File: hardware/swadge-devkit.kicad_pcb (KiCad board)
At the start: 2 copper layers, 63.7 x 100 mm, 60 parts, among them J1 USB_B_Micro, SW1 SW_SPDT, SW2 4-1437565-2, SW3 4-1437565-2, SW4 4-1437565-2, SW5 4-1437565-2, U1 ESP-12F, U2 MCP6001-OT, U3 MSA300, U4 AP1117-33, U5 BUS_PCIexpress, U6 DISP_OLED_UG-2864HSWEG01, U9 MMA8452Q

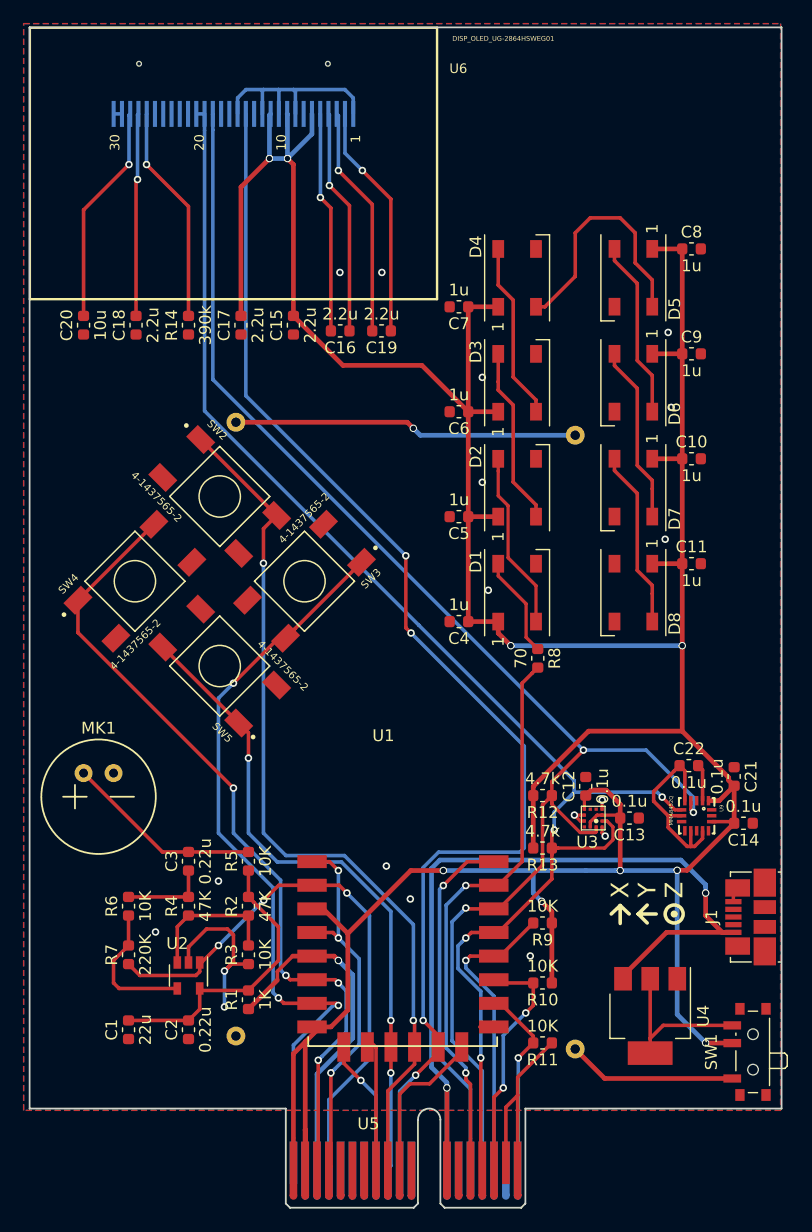
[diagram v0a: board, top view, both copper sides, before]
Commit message: Added SAO Moved mic out of the way of buttons Swapped 1.3" display for 0.96" display Linked vishay display instead of adafruit one
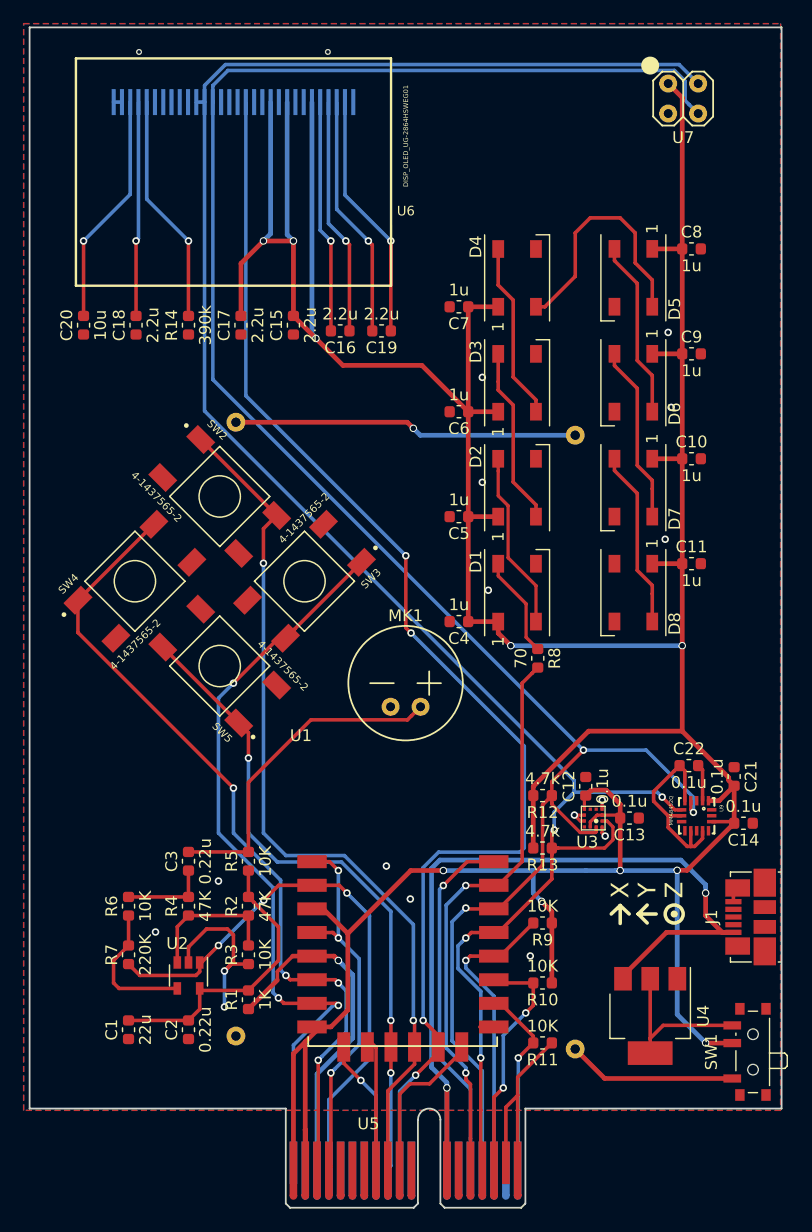
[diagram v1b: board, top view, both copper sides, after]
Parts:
- added U7: SAO, Swadge_Parts:SAO, F.Cu at (167.6, 52.1)
- U6: footprint Swadge_Parts:microbuilder-UG-2864HSWEG01_1.3_WRAPAROUND -> Swadge_Parts:microbuilder-UG-2864HSWEG01_0.96IN_WRAPAROUND
- moved MK1 27.7 mm to (145.4, 102.9), turned to 0 degrees
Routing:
- net SCL: track 129.1 -> 175.6 mm
- net SDA: track 126.9 -> 172.5 mm
- net +3V3: track 316.8 -> 349.8 mm, vias 9 -> 10
- net GND: track 74.9 -> 56.0 mm
- net Net-(C3-Pad2): track 16.7 -> 28.2 mm
- net Net-(C16-Pad1): track 19.1 -> 20.1 mm
- net Net-(C20-Pad2): track 18.8 -> 19.8 mm
- net Net-(C18-Pad2): track 17.2 -> 18.2 mm
- net MOSI: track 107.4 -> 108.4 mm
- net Net-(C19-Pad2): track 19.6 -> 20.6 mm
- net Net-(C19-Pad1): track 20.0 -> 21.0 mm
- net Net-(C16-Pad2): track 18.8 -> 19.8 mm
- net Net-(R14-Pad2): track 18.6 -> 19.6 mm
- net (no net): vias 2 -> 0

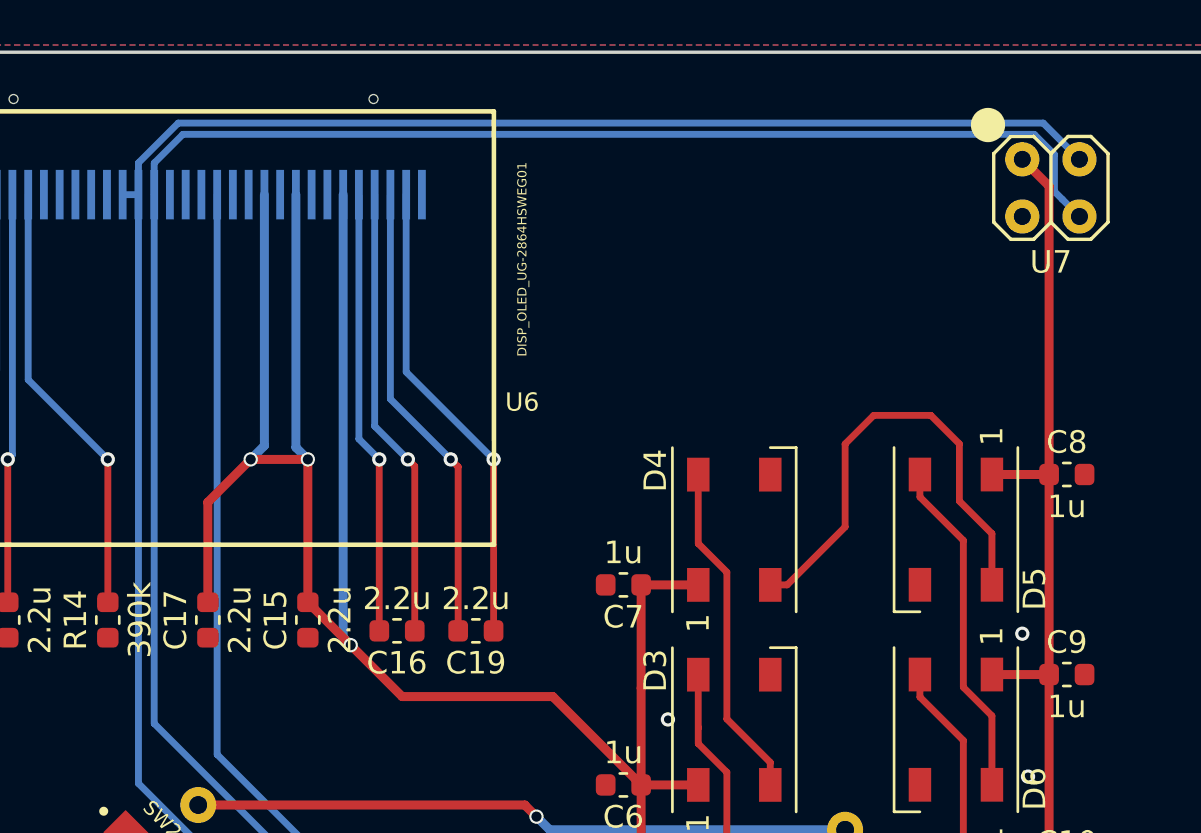
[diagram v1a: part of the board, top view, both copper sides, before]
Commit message: Added magfest logo & PCB color swatches
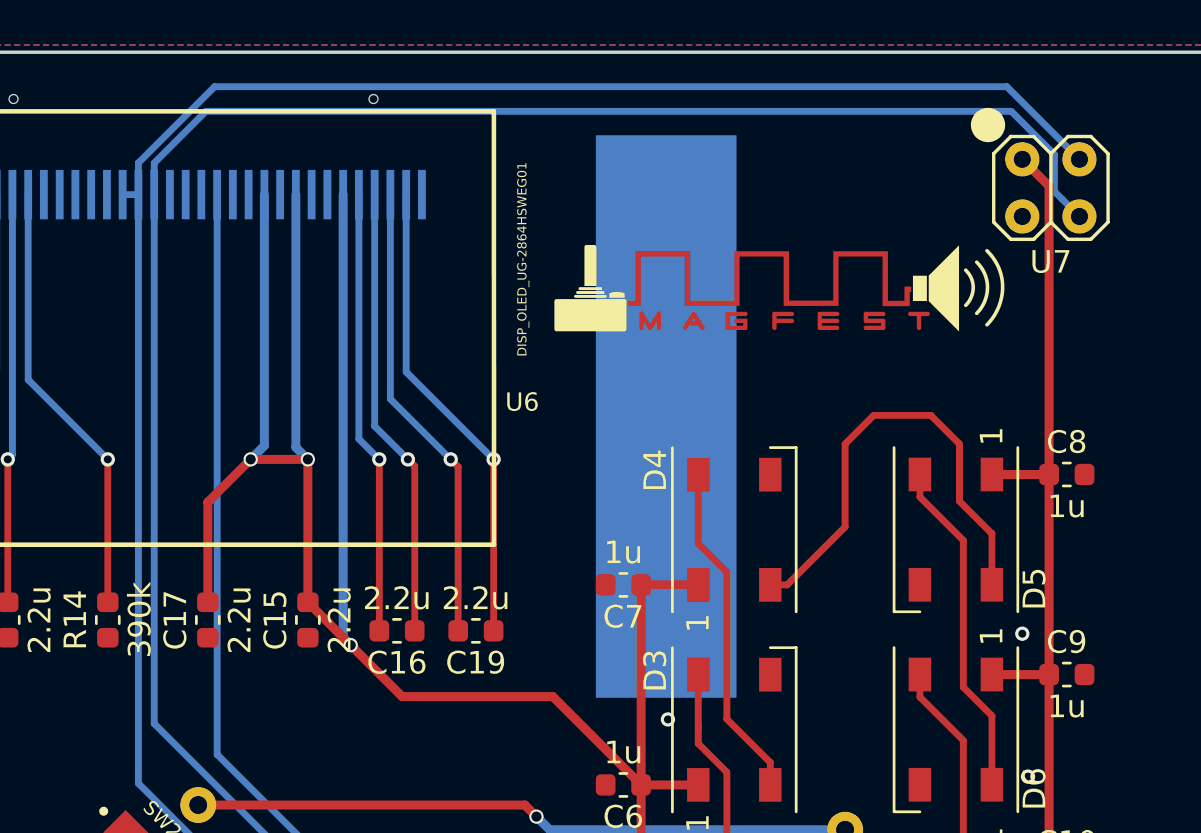
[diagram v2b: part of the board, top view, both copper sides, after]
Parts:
- added svg2mod: G***, Swadge_Parts:pcb_color_swatches, B.Cu at (154.9, 63.5)
- added svg2mod: G***, Swadge_Parts:MAGFEST_logo_centered_final, F.Cu at (156.8, 57.8)
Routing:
- net SDA: track 172.5 -> 173.9 mm
- net SCL: track 175.6 -> 176.4 mm

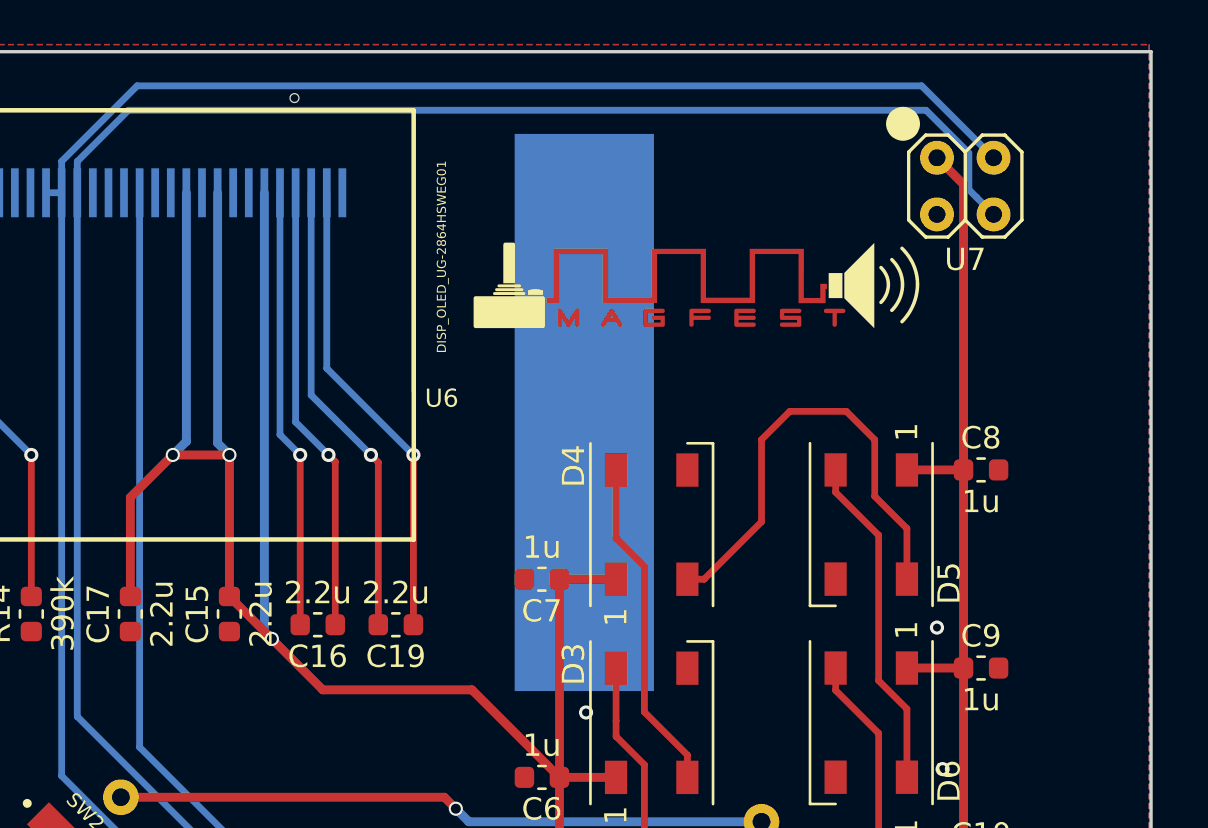
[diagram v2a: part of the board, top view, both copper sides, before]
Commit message: Added digikey part numbers for passives Updated PCB color swatch, logo Added name & version to PCB
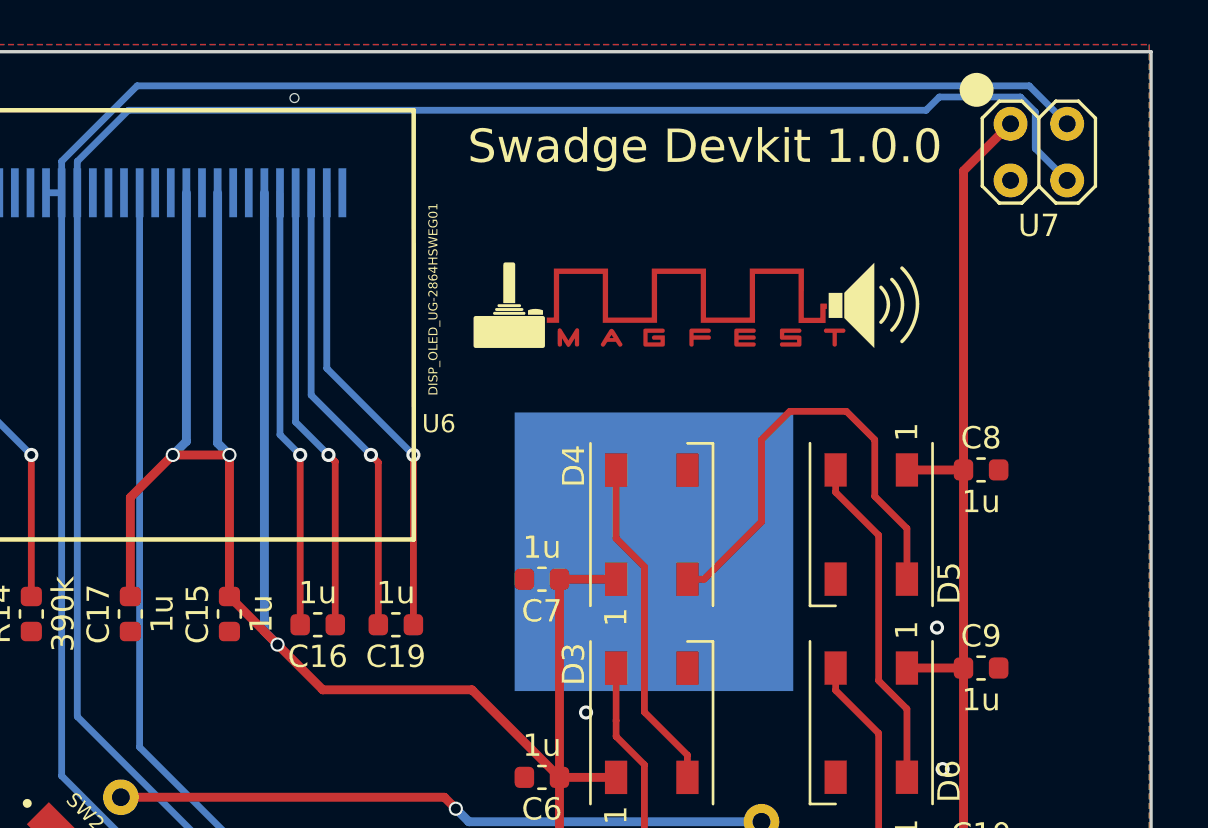
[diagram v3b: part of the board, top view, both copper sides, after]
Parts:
- C15, C16, C17, C19: value 2.2u -> 1u
- moved U7 3.64 mm to (170.9, 50.5)
- moved svg2mod 0.89 mm to (156.8, 58.7)
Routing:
- net SCL: track 176.4 -> 179.6 mm
- net SDA: track 173.9 -> 176.5 mm
- net +3V3: track 349.8 -> 352.1 mm
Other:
- board text added: "Swadge Devkit 1.0.0"

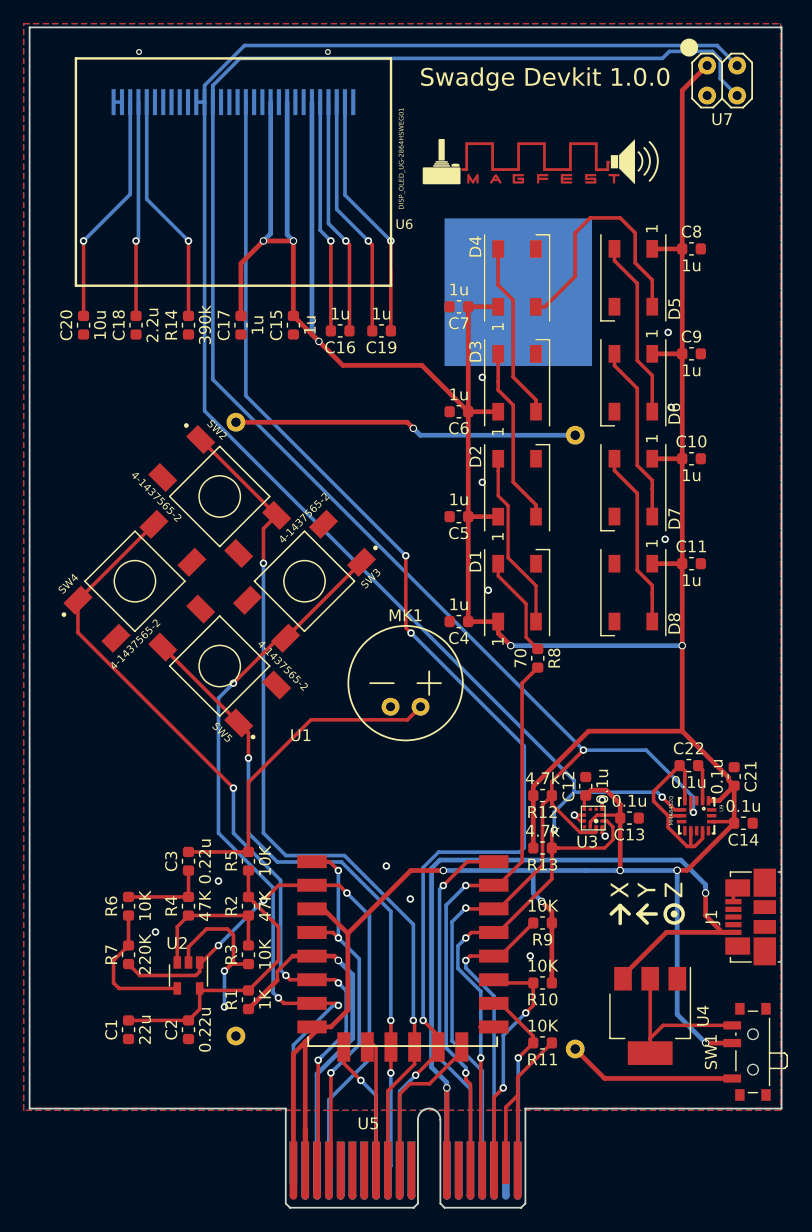
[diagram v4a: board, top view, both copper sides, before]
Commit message: #14 Replaced ESP-12F with ESP-WROOM-02D
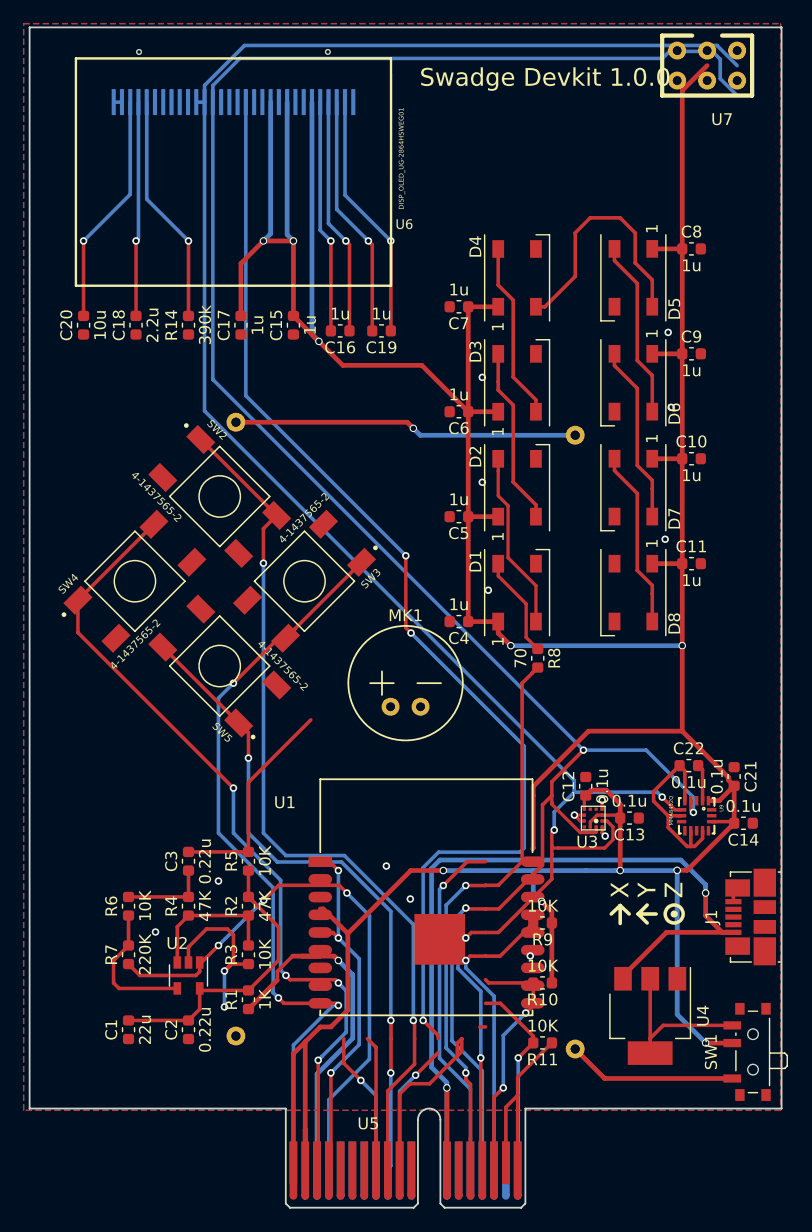
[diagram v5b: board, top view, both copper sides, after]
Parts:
- removed R12, R13: 4.7k, Swadge_Parts:R_0603_1608Metric
- removed svg2mod: G***, Swadge_Parts:pcb_color_swatches
- removed svg2mod: G***, Swadge_Parts:MAGFEST_logo_centered_final
- U1: value ESP-12F -> ESP-13-WROOM-02D; footprint Swadge_Parts:ESP-12E_SMD -> Swadge_Parts:ESP-13-WROOM-02
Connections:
- R10 pad 2: GPIO2 -> SDA
- R11 pad 2: GPIO15 -> _RES
- R9 pad 2: GPIO0 -> SCL
- U1 pad 1: REST -> +3V3
- U1 pad 10: GPIO15 -> SW2
- U1 pad 11: GPIO2 -> RX
- U1 pad 12: GPIO0 -> TX
- U1 pad 13: SDA -> GND
- U1 pad 14: SCL -> SW5
- U1 pad 15: RX -> REST
- U1 pad 16: TX -> ADC_PIN
- U1 pad 17: CS0 -> REST
- U1 pad 18: MISO -> GND
- U1 pad 2: ADC_PIN -> +3V3
- U1 pad 3: +3V3 -> AUD_PWR
- U1 pad 4: REST -> SW4
- U1 pad 5: AUD_PWR -> SW3
- U1 pad 6: SW4 -> _RES
- U1 pad 7: SW3 -> SDA
- U1 pad 8: +3V3 -> SCL
- U5 pad A10: MOSI -> _RES
- U5 pad A16: GPIO0 -> Net-(U5-PadA16)
- U5 pad A18: GPIO15 -> Net-(U5-PadA18)
- U5 pad A8: CS0 -> Net-(U5-PadA8)
- U5 pad B10: SCLK -> Net-(U5-PadB10)
- U5 pad B16: GPIO2 -> Net-(U5-PadB16)
- U5 pad B8: MISO -> Net-(U5-PadB8)
- U6 pad 13: (no net) -> GND
- U6 pad 14: MOSI -> _RES
- U6 pad 16: (no net) -> GND
- U6 pad 17: (no net) -> GND
- U6 pad 21: (no net) -> GND
- U6 pad 22: (no net) -> GND
- U6 pad 23: (no net) -> GND
- U6 pad 24: (no net) -> GND
- U6 pad 25: (no net) -> GND
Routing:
- net _RES: track 0.00 -> 108.4 mm, vias 0 -> 4
- net MOSI: track 108.4 -> 0.00 mm, vias 4 -> 0
- net SCLK: track 15.8 -> 0.00 mm
- net Net-(U5-PadB10): track 0.00 -> 15.8 mm
- net Net-(U5-PadA8): track 0.00 -> 12.1 mm, vias 0 -> 1
- net CS0: track 12.1 -> 0.00 mm, vias 1 -> 0
- net Net-(U5-PadB8): track 0.00 -> 11.3 mm
- net MISO: track 11.3 -> 0.00 mm
- net Net-(C3-Pad2): track 28.2 -> 19.0 mm

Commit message: #9 #11 #13 #14 #15 Routed everything
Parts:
- added svg2mod: G***, Swadge_Parts:pcb_color_swatches, B.Cu at (154.9, 63.5)
- added svg2mod: G***, Swadge_Parts:MAGFEST_logo_centered_final, F.Cu at (157.0, 58.7)
- moved R9 27.5 mm to (133.0, 136.5), turned to 0 degrees
- moved R11 24.6 mm to (133.0, 127.9), turned to 0 degrees
- moved R10 24.3 mm to (133.0, 132.2), turned to 0 degrees
- moved U1 4.89 mm to (136.4, 122.6)
- moved R1 3.82 mm to (128.5, 128.3)
- moved R2 3.82 mm to (128.5, 120.4)
- moved R3 3.82 mm to (128.5, 124.5)
- moved R5 3.82 mm to (128.5, 116.6)
- moved U2 3.82 mm to (123.4, 126.2)
- moved C1 3.82 mm to (118.4, 130.8)
- moved C2 3.82 mm to (123.4, 130.8)
- moved C3 3.82 mm to (123.4, 116.6)
- moved R4 3.82 mm to (123.4, 120.4)
- moved R6 3.82 mm to (118.4, 120.4)
- moved R7 3.82 mm to (118.4, 124.5)
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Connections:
- U1 pad 10: SW2 -> SW4
- U1 pad 4: SW4 -> SW3
- U1 pad 5: SW3 -> SW2
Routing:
- net +5V: track 74.0 -> 45.1 mm
- net GND: track 55.5 -> 82.0 mm, vias 16 -> 19
- net GPIO0: track 25.7 -> 0.00 mm, vias 1 -> 0
- net GPIO2: track 21.3 -> 0.00 mm, vias 2 -> 0
- net SW5: track 55.5 -> 76.8 mm, vias 3 -> 4
- net GPIO15: track 17.0 -> 0.00 mm, vias 1 -> 0
- net +3V3: track 352.1 -> 335.5 mm, vias 10 -> 11
- net SW4: track 70.4 -> 86.9 mm, vias 4 -> 3
- net Net-(U5-PadB10): track 15.8 -> 0.00 mm
- net TX: track 29.6 -> 17.2 mm, vias 1 -> 3
- net Net-(U5-PadA8): track 12.1 -> 0.00 mm, vias 1 -> 0
- net Net-(U5-PadB8): track 11.3 -> 0.00 mm
- net SDA: track 176.5 -> 187.0 mm, vias 4 -> 3
- net SCL: track 179.6 -> 188.7 mm, vias 3 -> 5
- net REST: track 30.6 -> 39.2 mm, vias 3 -> 2
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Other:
- board text added: "Swadge Devkit 1.1.0"
- board text removed: "Swadge Devkit 1.0.0"
